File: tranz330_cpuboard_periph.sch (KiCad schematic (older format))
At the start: 21 parts, among them P1 CONN_01X20, P4 CONN_01X08, P5 CONN_01X06, U11 74HC04, U15 Z80DART, U2 M6242B, U20 DS1489, U28 DS14C88, U30 73K212AL, U4 Z80CTC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

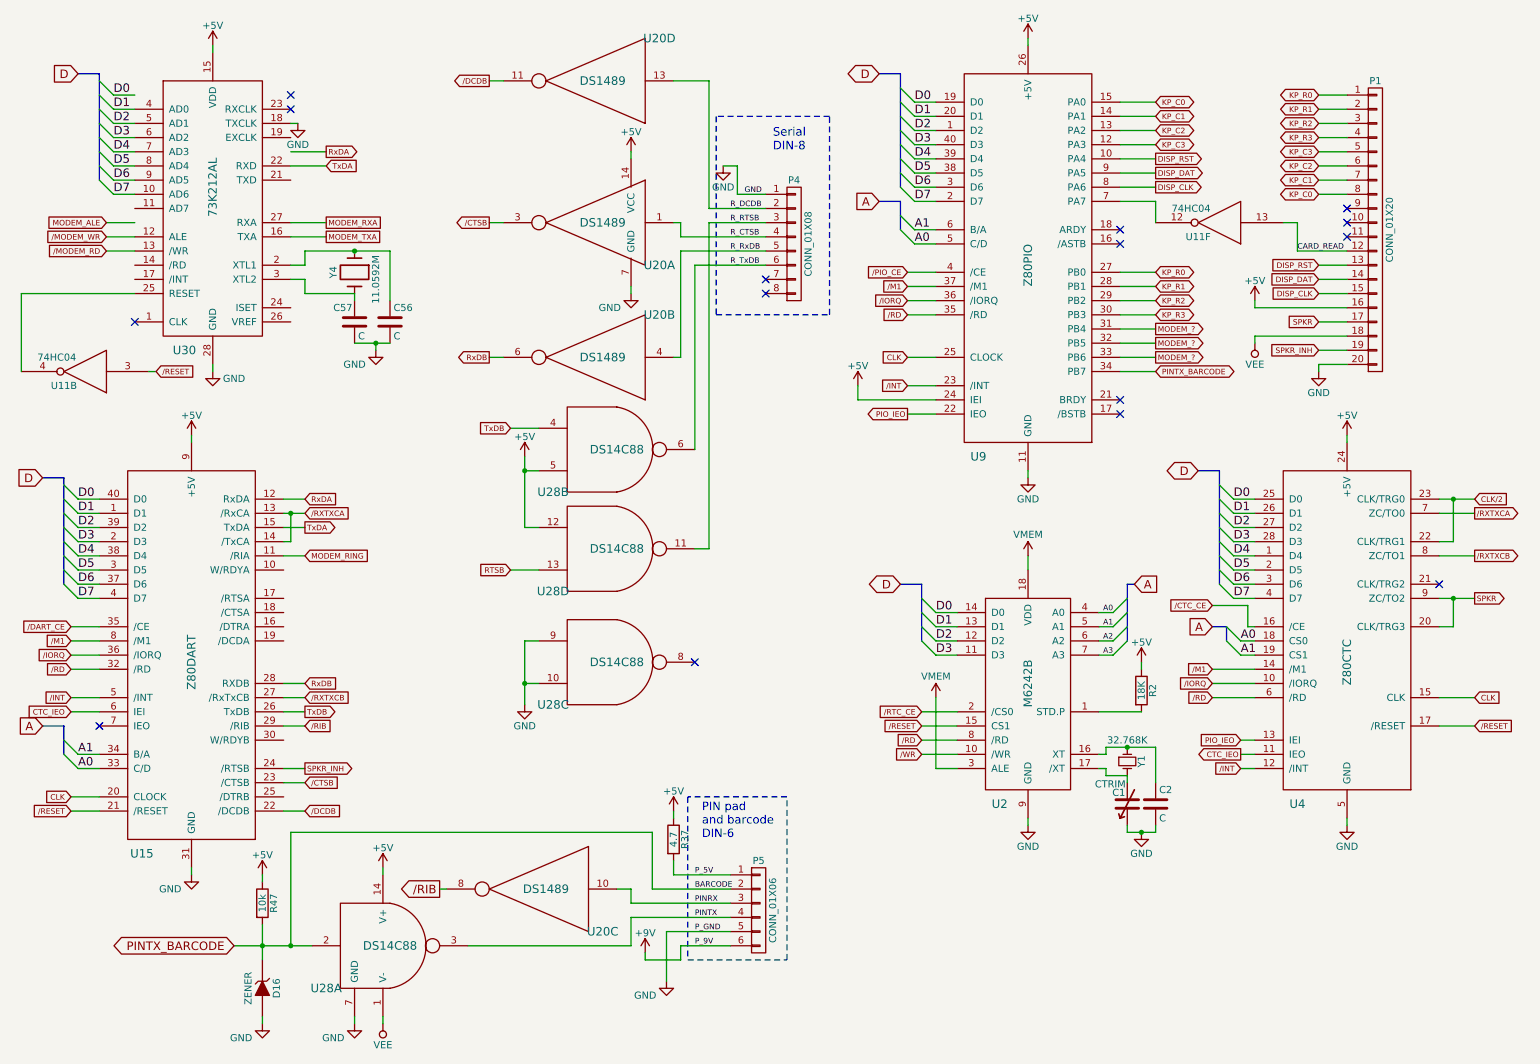
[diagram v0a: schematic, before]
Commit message: Fix /RTSB, better PDF output, trace missing DART and modem pins
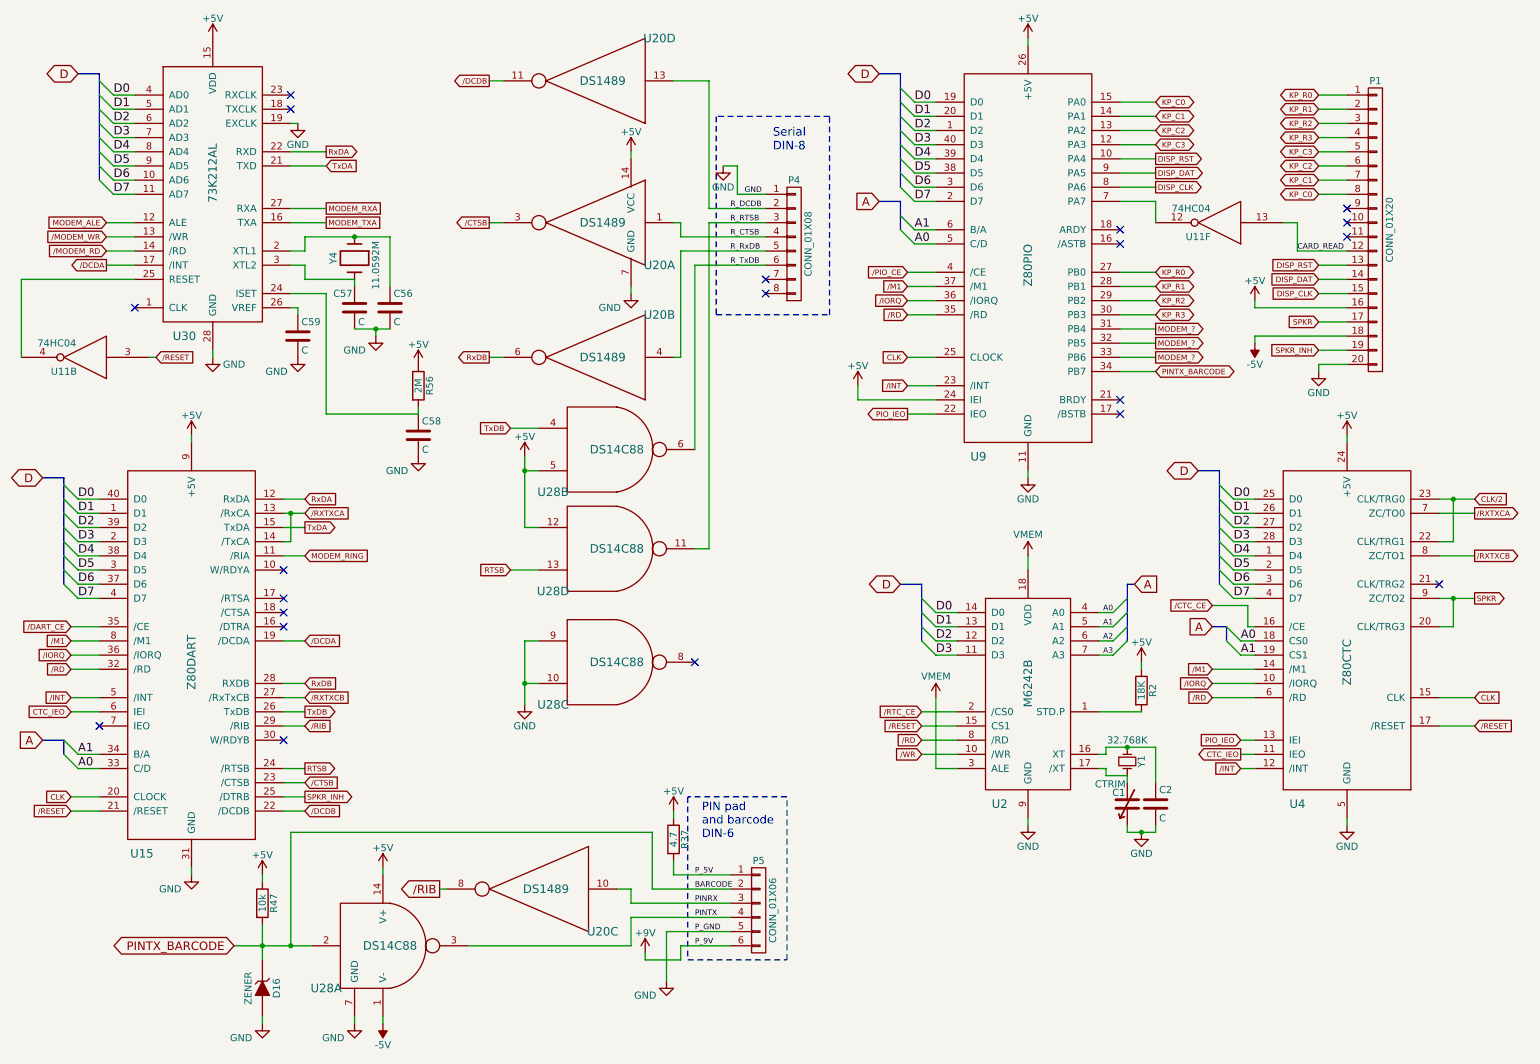
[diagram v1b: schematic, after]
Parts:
- added C58, C59: C, symbol C
- added R56: 2M, symbol R
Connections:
- net +5V: now also R56.1
- net /MODEM_RD: now also U30.14 (/RD); no longer U30.13 (/WR)
- net /MODEM_WR: now also U30.13 (/WR); no longer U30.12 (ALE)
- net D0: now also U30.4 (AD0)
- net D1: now also U30.5 (AD1); no longer U30.4 (AD0)
- net D2: now also U30.6 (AD2); no longer U30.5 (AD1)
- net D3: now also U30.7 (AD3); no longer U30.6 (AD2)
- net D4: now also U30.8 (AD4); no longer U30.7 (AD3)
- net D5: now also U30.9 (AD5); no longer U30.8 (AD4)
- net D6: now also U30.10 (AD6); no longer U30.9 (AD5)
- net D7: now also U30.11 (AD7); no longer U30.10 (AD6)
- net GND: now also U30.19 (EXCLK), C58.2, C59.2; no longer U30.18 (TXCLK)
- net MODEM_ALE: now also U30.12 (ALE)
- net RTSB: now also U15.24 (/RTSB)
- net RxDA: now also U30.22 (RXD)
- net SPKR_INH: now also U15.25 (/DTRB); no longer U15.24 (/RTSB)
- net TxDA: now also U30.21 (TXD); no longer U30.22 (RXD)
- net /DCDA: now reaches U15.19 (/DCDA)
- net /DCDA: now also U30.17 (/INT)
- net at U30.24 (ISET): now also C58.1, R56.2
- net at U30.26 (VREF): now also C59.1
- net VEE renamed -5V
- no-connect marks 15 -> 20
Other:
- moved on the sheet: C56, C57, U11B, U30, Y4
